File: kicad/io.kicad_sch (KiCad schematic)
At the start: 25 parts, among them J15 IN1, J16 IN2, J17 IN3, J18 IN4, J19 1-Wire 1, J20 1-Wire 2, J21 1-Wire 3, J22 I2C 1, J23 I2C 2, J24 Display

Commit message: kicad: drop the third 1-Wire terminal
Two terminals are enough for the bus (several sensors per terminal).
Saves one AKL 101-03 (0.39 EUR/board) and board edge space.

Co-Authored-By: Claude Opus 5.5 <noreply@anthropic.com>
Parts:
- removed J21: 1-Wire 3, TerminalBlock_Phoenix:TerminalBlock_Phoenix_MKDS-1,5-3-5.08_1x03_P5.08mm_Horizontal, symbol Connector:Screw_Terminal_01x03
- removed J23: I2C 2, Connector_PinHeader_2.54mm:PinHeader_1x04_P2.54mm_Vertical, symbol Connector_Generic:Conn_01x04
- removed J24: Display, Connector_PinHeader_2.54mm:PinHeader_1x10_P2.54mm_Vertical, symbol Connector_Generic:Conn_01x10
- added J21: I2C 1, Connector_PinHeader_2.54mm:PinHeader_1x04_P2.54mm_Vertical, symbol Connector_Generic:Conn_01x04
- added J23: Display, Connector_PinHeader_2.54mm:PinHeader_1x10_P2.54mm_Vertical, symbol Connector_Generic:Conn_01x10
- J22: value I2C 1 -> I2C 2
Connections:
- net +3V3: now also J21.2 (Pin_2), J23.2 (Pin_2)
- net DISP_BL: now also J23.10 (Pin_10)
- net GND: now also J21.1 (Pin_1), J23.1 (Pin_1)
- net GPIO10_MOSI: now also J23.4 (Pin_4)
- net GPIO11_SCLK: now also J23.3 (Pin_3)
- net GPIO24_DISP_RST: now also J23.9 (Pin_9)
- net GPIO25_DISP_DC: now also J23.8 (Pin_8)
- net GPIO2_SDA: now also J21.4 (Pin_4)
- net GPIO3_SCL: now also J21.3 (Pin_3)
- net GPIO7_CE1: now also J23.7 (Pin_7)
- net GPIO8_CE0: now also J23.6 (Pin_6)
- net GPIO9_MISO: now also J23.5 (Pin_5)

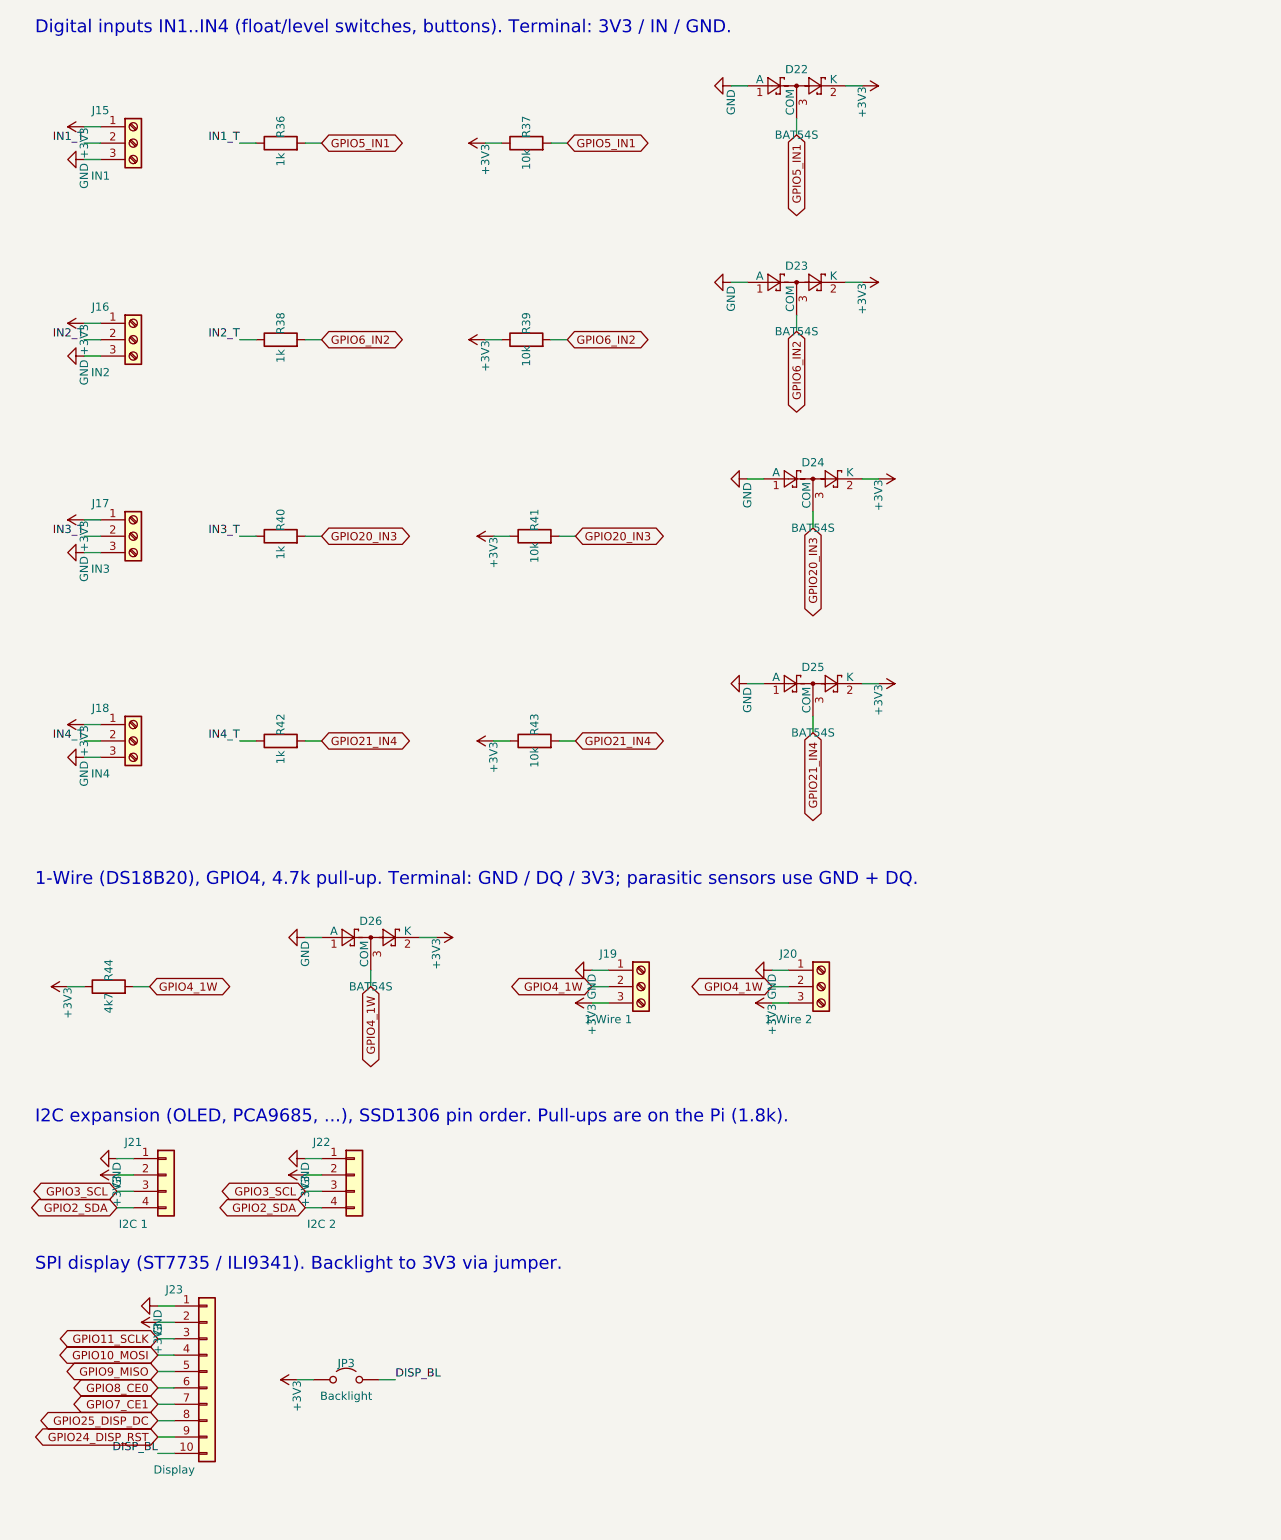
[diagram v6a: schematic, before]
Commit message: kicad: restore the hand-edited schematic from KiCad local history
f617249 overwrote the schematic that had been tidied by hand in
eeschema (labels replaced by wires and junctions) with a regenerated
draft and new symbol UUIDs. Restore all sheets and the project file
from KiCad's local history snapshot eb84d42 (2026-09-30 14:45).
Connectivity matches that snapshot; all 153 symbols link to the
footprints in aquaPCB.kicad_pcb again. The third 1-Wire terminal (J21)
is still in the schematic and has to be deleted in eeschema.

Co-Authored-By: Claude Opus 5.5 <noreply@anthropic.com>
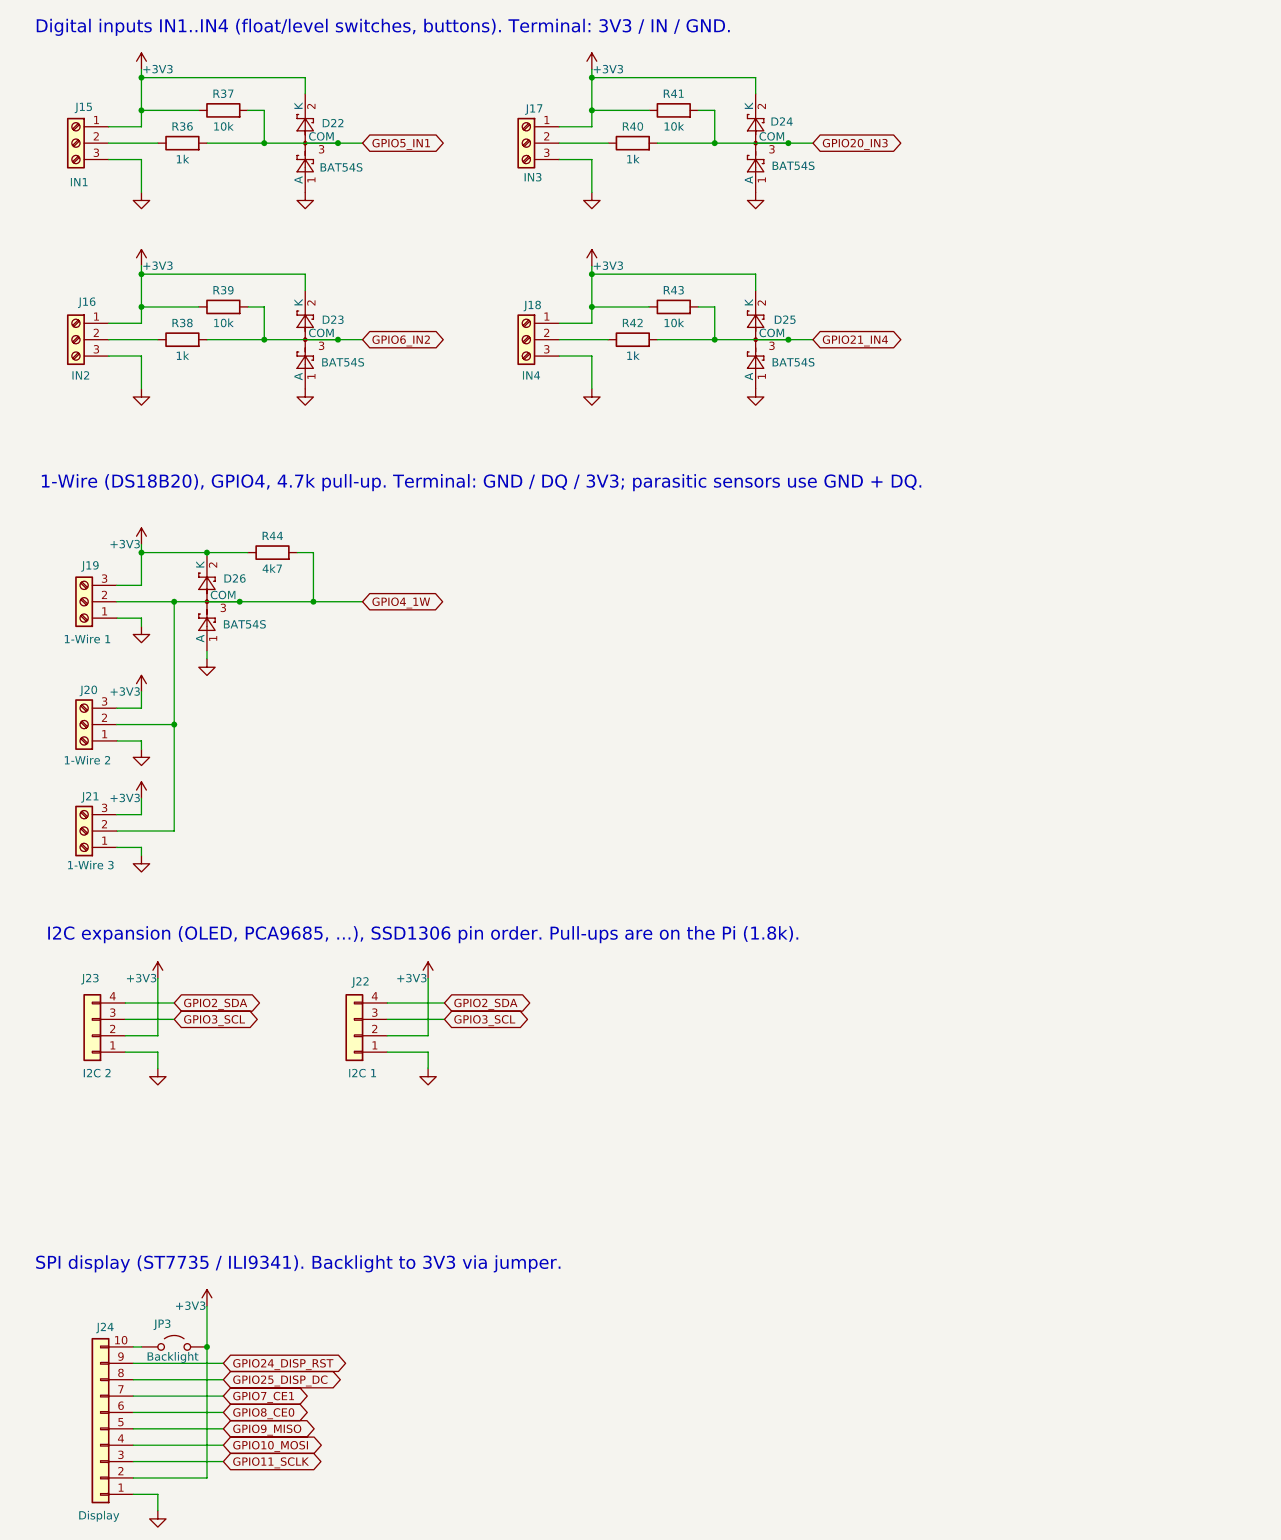
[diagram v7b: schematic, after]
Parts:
- removed J21: I2C 1, Connector_PinHeader_2.54mm:PinHeader_1x04_P2.54mm_Vertical, symbol Connector_Generic:Conn_01x04
- removed J23: Display, Connector_PinHeader_2.54mm:PinHeader_1x10_P2.54mm_Vertical, symbol Connector_Generic:Conn_01x10
- added J21: 1-Wire 3, TerminalBlock_Phoenix:TerminalBlock_Phoenix_MKDS-1,5-3-5.08_1x03_P5.08mm_Horizontal, symbol Connector:Screw_Terminal_01x03
- added J23: I2C 2, Connector_PinHeader_2.54mm:PinHeader_1x04_P2.54mm_Vertical, symbol Connector_Generic:Conn_01x04
- added J24: Display, Connector_PinHeader_2.54mm:PinHeader_1x10_P2.54mm_Vertical, symbol Connector_Generic:Conn_01x10
- J22: value I2C 2 -> I2C 1
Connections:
- net DISP_BL is gone; now on net +3V3: JP3.2 (B)
- net +3V3: now also J21.3 (Pin_3), J23.2 (Pin_2), J24.2 (Pin_2); no longer JP3.1 (A)
- net GND: now also J21.1 (Pin_1), J23.1 (Pin_1), J24.1 (Pin_1)
- net GPIO10_MOSI: now also J24.4 (Pin_4)
- net GPIO11_SCLK: now also J24.3 (Pin_3)
- net GPIO24_DISP_RST: now also J24.9 (Pin_9)
- net GPIO25_DISP_DC: now also J24.8 (Pin_8)
- net GPIO2_SDA: now also J23.4 (Pin_4)
- net GPIO3_SCL: now also J23.3 (Pin_3)
- net GPIO4_1W: now also J21.2 (Pin_2)
- net GPIO7_CE1: now also J24.7 (Pin_7)
- net GPIO8_CE0: now also J24.6 (Pin_6)
- net GPIO9_MISO: now also J24.5 (Pin_5)
- net IN1_T: no longer names the net of J15.2 (Pin_2), R36.1
- net IN2_T: no longer names the net of J16.2 (Pin_2), R38.1
- net IN3_T: no longer names the net of J17.2 (Pin_2), R40.1
- net IN4_T: no longer names the net of J18.2 (Pin_2), R42.1
- new net: J24.10 (Pin_10), JP3.1 (A)

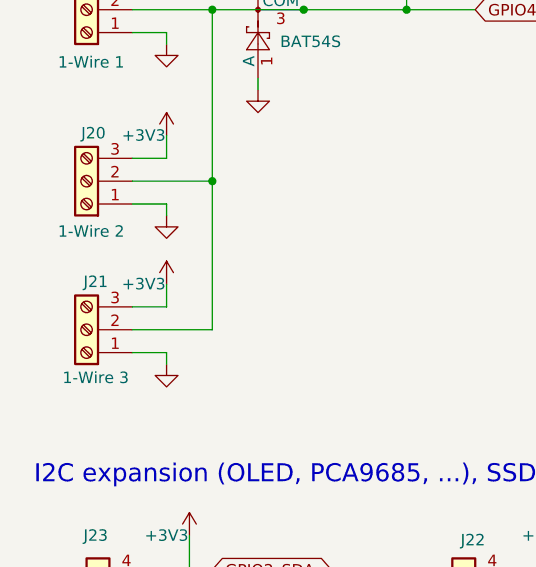
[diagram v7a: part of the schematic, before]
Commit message: kicad: remove the third 1-Wire terminal (J21)
Deleted in eeschema; connectivity otherwise unchanged (checked against
the restored netlist).

Co-Authored-By: Claude Opus 5.5 <noreply@anthropic.com>
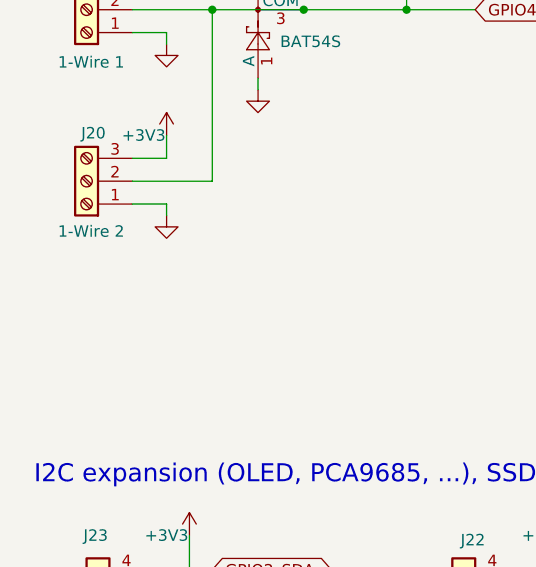
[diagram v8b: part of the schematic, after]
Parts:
- removed J21: 1-Wire 3, TerminalBlock_Phoenix:TerminalBlock_Phoenix_MKDS-1,5-3-5.08_1x03_P5.08mm_Horizontal, symbol Connector:Screw_Terminal_01x03
